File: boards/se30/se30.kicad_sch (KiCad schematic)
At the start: 54 parts, among them J3 Conn_01x07, J3 Conn_02x05_Odd_Even, U2 ENC624J600-PT, U3 74LVC2G17, U4 ATF1502AS-xAx44, U4 SST39SF010, U5 LD1117S33TR_SOT223, Y1 25MHz

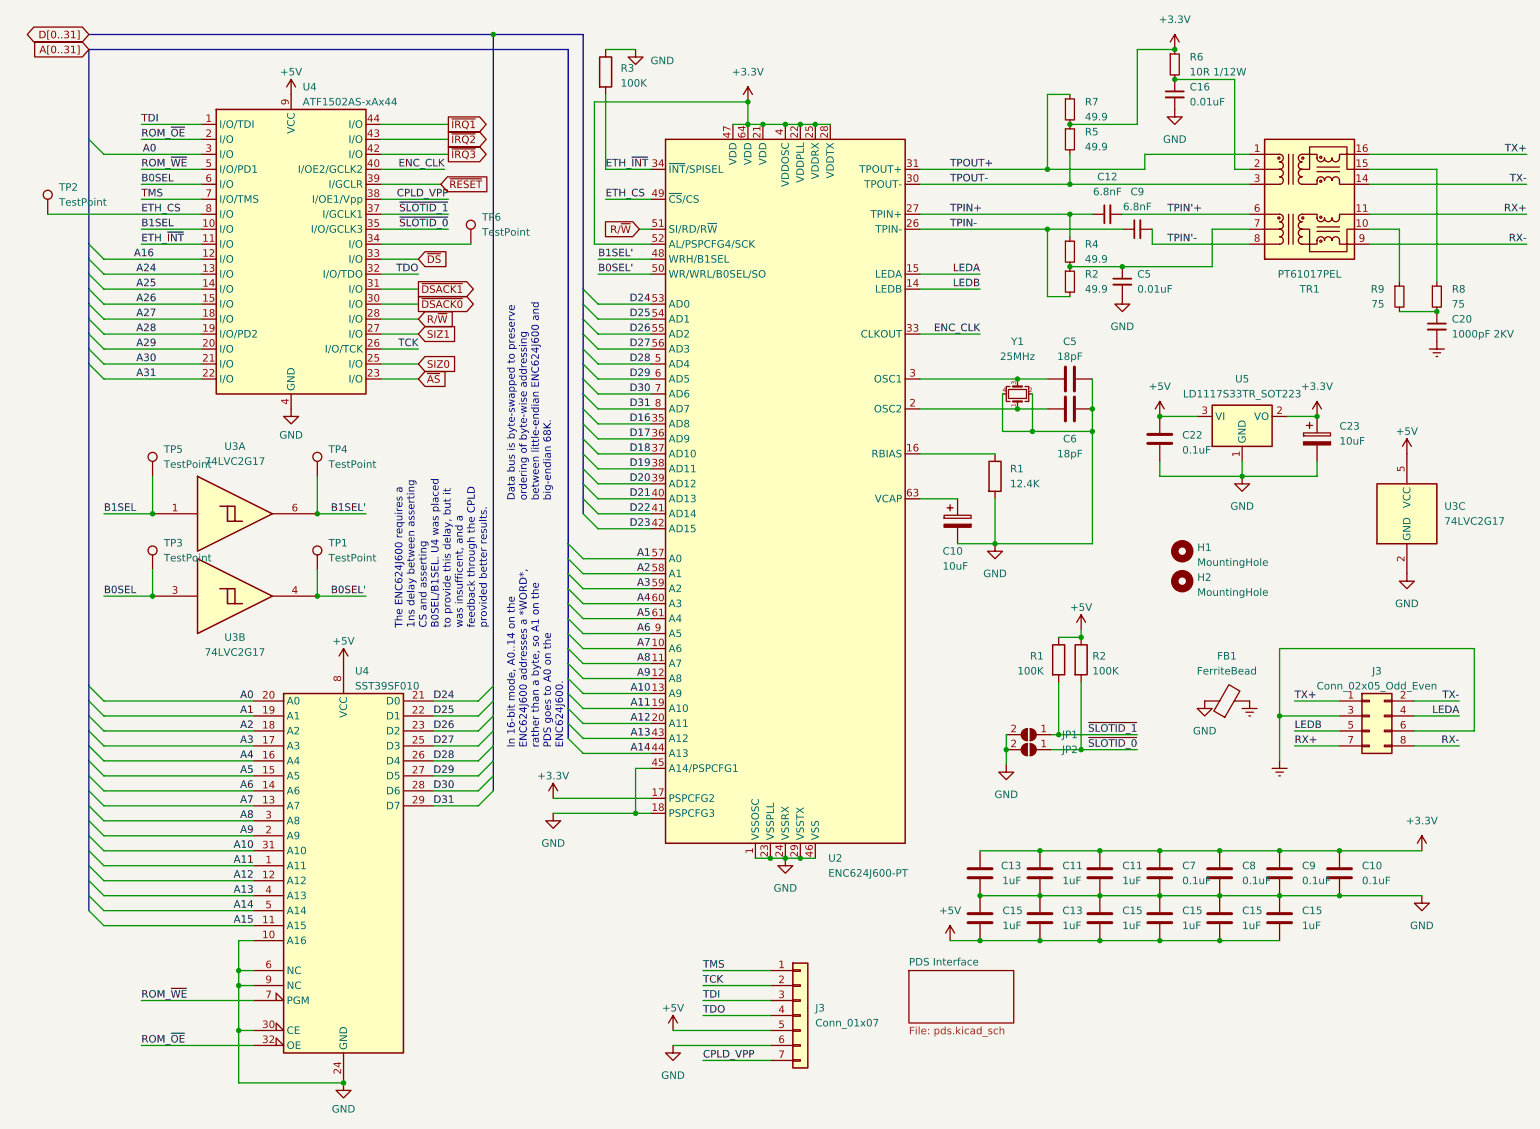
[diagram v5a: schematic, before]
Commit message: SE30: Remove delay buffer on /BxSEL lines
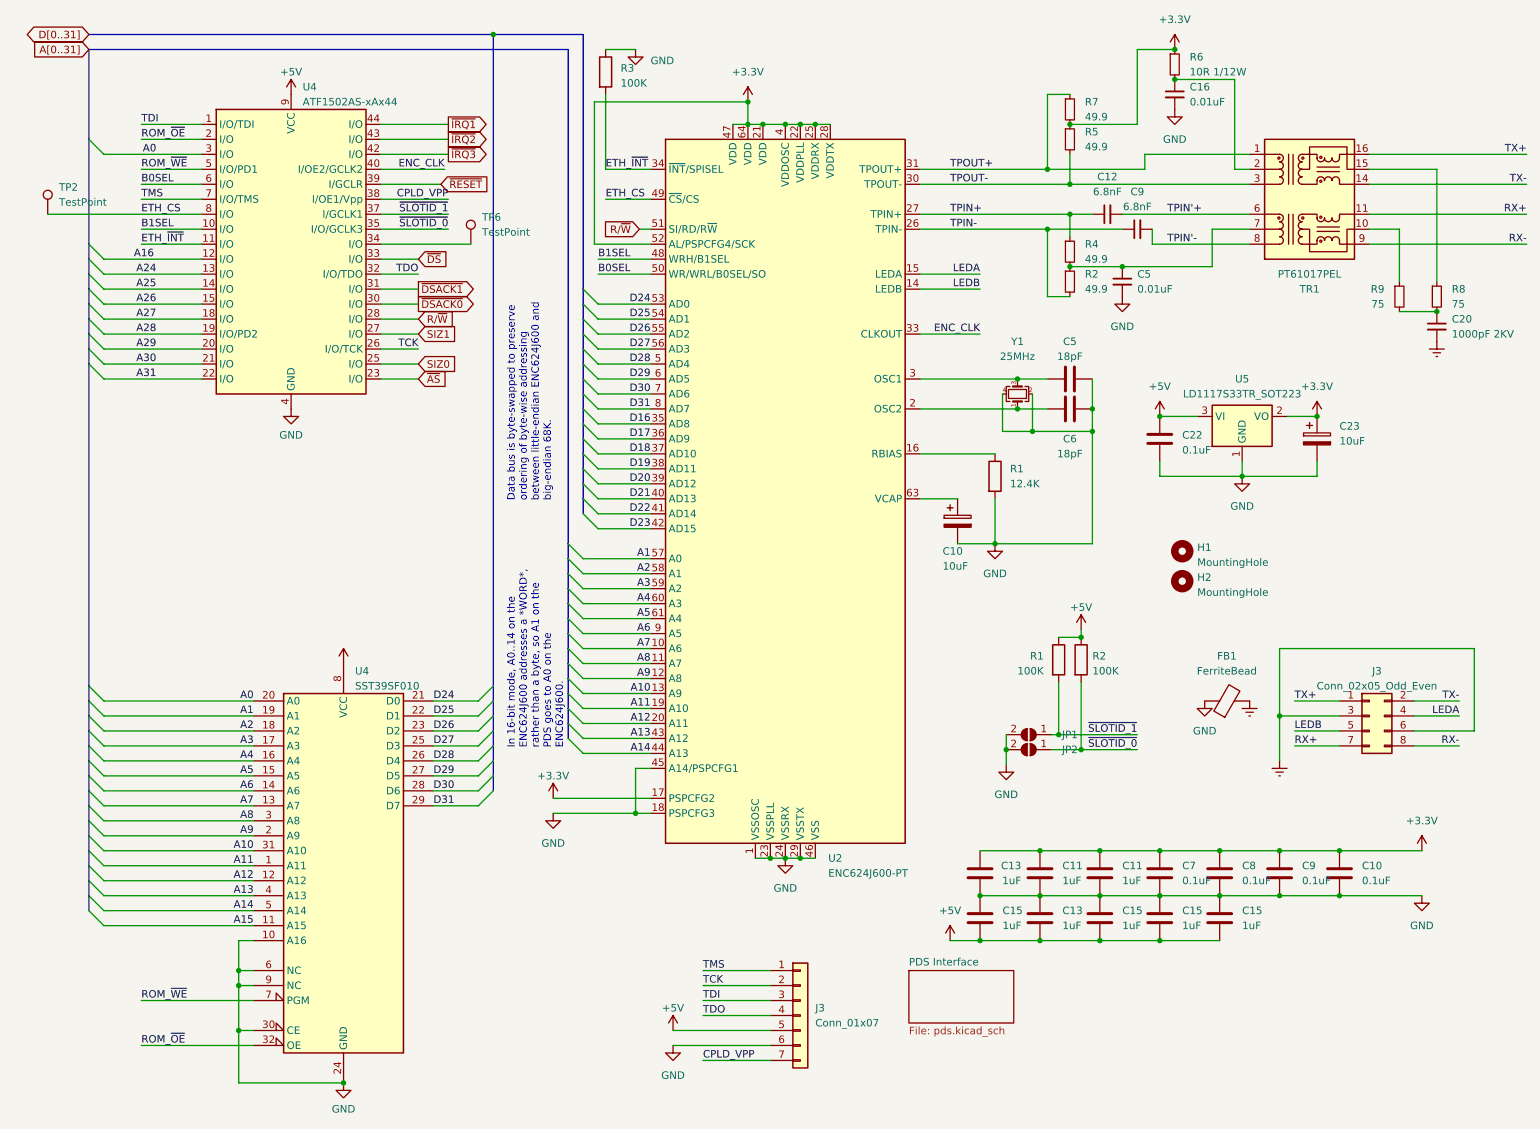
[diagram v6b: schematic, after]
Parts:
- removed C15: 1uF, Capacitor_SMD:C_0805_2012Metric_Pad1.18x1.45mm_HandSolder, symbol Device:C
- removed TP1, TP3, TP4, TP5: TestPoint, TestPoint:TestPoint_Pad_D1.0mm, symbol Connector:TestPoint
- removed U3: 74LVC2G17, Package_TO_SOT_SMD:SOT-363_SC-70-6, symbol 74xGxx:74LVC2G17
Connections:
- net B0SEL' is gone; now on net B0SEL: U2.50 (WR/WRL/B0SEL/SO)
- net B1SEL' is gone; now on net B1SEL: U2.48 (WRH/B1SEL)
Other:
- moved on the sheet: C15
